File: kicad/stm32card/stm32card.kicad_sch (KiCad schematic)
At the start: 48 parts, among them SW1 TSD003A04126A02, SW2 TSD003A04126A02, SW3 TSD003A04126A02, SW4 TSD003A04126A02, SW5 TSD003A04126A02, SW6 TSD003A04126A02, SW8 TSD003A04126A02, U2 MT9216, U3 N096-1608TBBIG11-H13, U4 STM32F103C8T6

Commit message: rev1a
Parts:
- removed BAT1, BAT2, BAT3, BAT4: 2997, 2997_KEY, symbol 2025-02-07_04-30-39:2997
- removed C10, C20, C6: 10uF, Capacitor_SMD:C_0603_1608Metric, symbol Device:C
- removed C21: 100nF, Capacitor_SMD:C_0603_1608Metric, symbol Device:C
- removed R3: 0, Resistor_SMD:R_0603_1608Metric, symbol Device:R
- removed SW8: TSD003A04126A02, easyeda2kicad:SW-SMD_4P-L6.0-W6.0-P4.50-LS8.6, symbol easyeda2kicad:TSD003A04126A02
- added J1: USB_C_Receptacle_PowerOnly_6P, indigos_kicad_lib:SAMESKY_UJC-H-G-SMT-2-P6-TR, symbol Connector:USB_C_Receptacle_PowerOnly_6P
- added R1, R2: 5.1k, Resistor_SMD:R_0603_1608Metric, symbol Device:R
- added SWCLK1: SWCLK, TestPoint:TestPoint_Pad_D2.0mm, symbol Connector:TestPoint
- added SWDIO1: SWDIO, TestPoint:TestPoint_Pad_D2.0mm, symbol Connector:TestPoint
- added TP1: 675_positive, TestPoint:TestPoint_Pad_4.0x4.0mm, symbol Connector:TestPoint
- added TP_mosi1, TP_sck1: TestPoint, TestPoint:TestPoint_Pad_D2.0mm, symbol Connector:TestPoint
- added TestPoint_gnd1: TestPoint_gnd, TestPoint:TestPoint_Pad_D2.0mm, symbol Connector:TestPoint
- added U2, U3: LM66100DCK, Package_TO_SOT_SMD:SOT-363_SC-70-6, symbol Power_Management:LM66100DCK
- added U6: ~, Library:battery_holder, symbol battery_holder:quad_675
- added tst_nrst1: tst_nrst, TestPoint:TestPoint_Pad_D2.0mm, symbol Connector:TestPoint
- added unreg_vcc1: unreg_vcc, TestPoint:TestPoint_Pad_D2.0mm, symbol Connector:TestPoint
- C1: value 4.7uF -> 10uF
- C8: value 10uF -> 2.2uF
- L1: footprint Inductor_SMD:L_0603_1608Metric -> indigos_kicad_lib:IND-SMD_L5.8-W5.2
- R3: renamed from R1; footprint Resistor_SMD:R_0603_1608Metric -> Resistor_SMD:R_0805_2012Metric
- R4: renamed from R2; value 100k 1% -> 100k .01%; footprint Resistor_SMD:R_0603_1608Metric -> Resistor_SMD:R_0805_2012Metric
- renumbered C3 to C10, C19 to C11, C17 to C15, C15 to C16, C16 to C17, C5 to C2, C4 to C3, C7 to C4, C9 to C5, C11 to C6, C2 to C9, R11 to R10, R12 to R11, R7 to R12, R9 to R13, R4 to R5, R5 to R6, R8 to R7, R10 to R8, R6 to R9, U2 to U1, U3 to U5, SW4 to b_a1, SW6 to b_b1, SW2 to b_down1, SW5 to b_left1, SW3 to b_right1, SW1 to b_up1
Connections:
- net +3V0: now also C8.2; no longer C8.1
- net GND: now also C8.1, J1.A12 (GND), J1.B12 (GND), J1.S1 (SHIELD), R1.2, R2.2, TestPoint_gnd1.1, U2.2 (GND), U3.2 (GND), U3.5 (ST), U6.1 (gnd_1), U6.2 (gnd_2), U6.3 (gnd_3), U6.4 (gnd_4); no longer C8.2
- net spi1_mosi: now also TP_mosi1.1
- net spi1_sck: now also TP_sck1.1
- net in_button_a: now reaches C17.2, b_a1.4
- net in_button_a: now also U4.26 (PB13), b_a1.3
- net in_button_b: now reaches C18.2, b_b1.4
- net in_button_b: now also U4.27 (PB14), b_b1.3
- net in_button_down: now reaches C14.2, b_down1.4
- net in_button_down: now also U4.10 (PA0-WKUP), b_down1.3
- net in_button_left: now reaches C15.2, b_left1.4
- net in_button_left: now also U4.12 (PA2), b_left1.3
- net in_button_up: now reaches C13.2, b_up1.4
- net in_button_up: now also U4.13 (PA3), b_up1.3
- net in_button_right: now reaches U4.11 (PA1)
- net in_button_right: now also C16.2, b_right1.3, b_right1.4
- net power_info: now reaches U4.25 (PB12)
- net power_info: now also U2.5 (ST)
- net at U4.34 (PA13): now also SWDIO1.1
- net at U4.37 (PA14): now also SWCLK1.1
- net at U4.42 (PB6): no longer U5.7 (CS)
- net at U4.43 (PB7): no longer U5.6 (RESET)
- net at U4.45 (PB8): no longer U5.5 (RS)
- net unregulated_vcc: now reaches C1.1, U1.1 (VIN), U1.3 (EN)
- net unregulated_vcc: now also U2.6 (VOUT), U3.6 (VOUT), unreg_vcc1.1
- net button_a: no longer names the net of U4.40 (PB4)
- net button_a: no longer b_a1.3
- net button_b: no longer names the net of U4.41 (PB5)
- net button_b: no longer b_b1.3
- net button_down renamed lcd_reset
- net lcd_reset: now also U5.6 (RESET); no longer b_down1.3
- net button_left renamed lcd_cs
- net lcd_cs: now also U5.7 (CS); no longer b_left1.3
- net button_right: no longer names the net of U4.39 (PB3)
- net button_right: no longer b_right1.3
- net button_up renamed lcd_dataselect
- net lcd_dataselect: now also U5.5 (RS); no longer b_up1.3
- net reset_button: no longer names the net of C11.1, U4.7 (NRST)
- net reset_button: now also tst_nrst1.1
- new net: TP1.1, U2.1 (VIN), U3.3 (~{CE})
- new net: J1.B5 (CC2), R1.1
- new net: J1.A9 (VBUS), J1.B9 (VBUS), U2.3 (~{CE}), U3.1 (VIN)
- new net: J1.A5 (CC1), R2.1
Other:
- moved on the sheet: C1, C10, C13, C14, C15, C16, C17, C18, C2, C3, C4, C5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

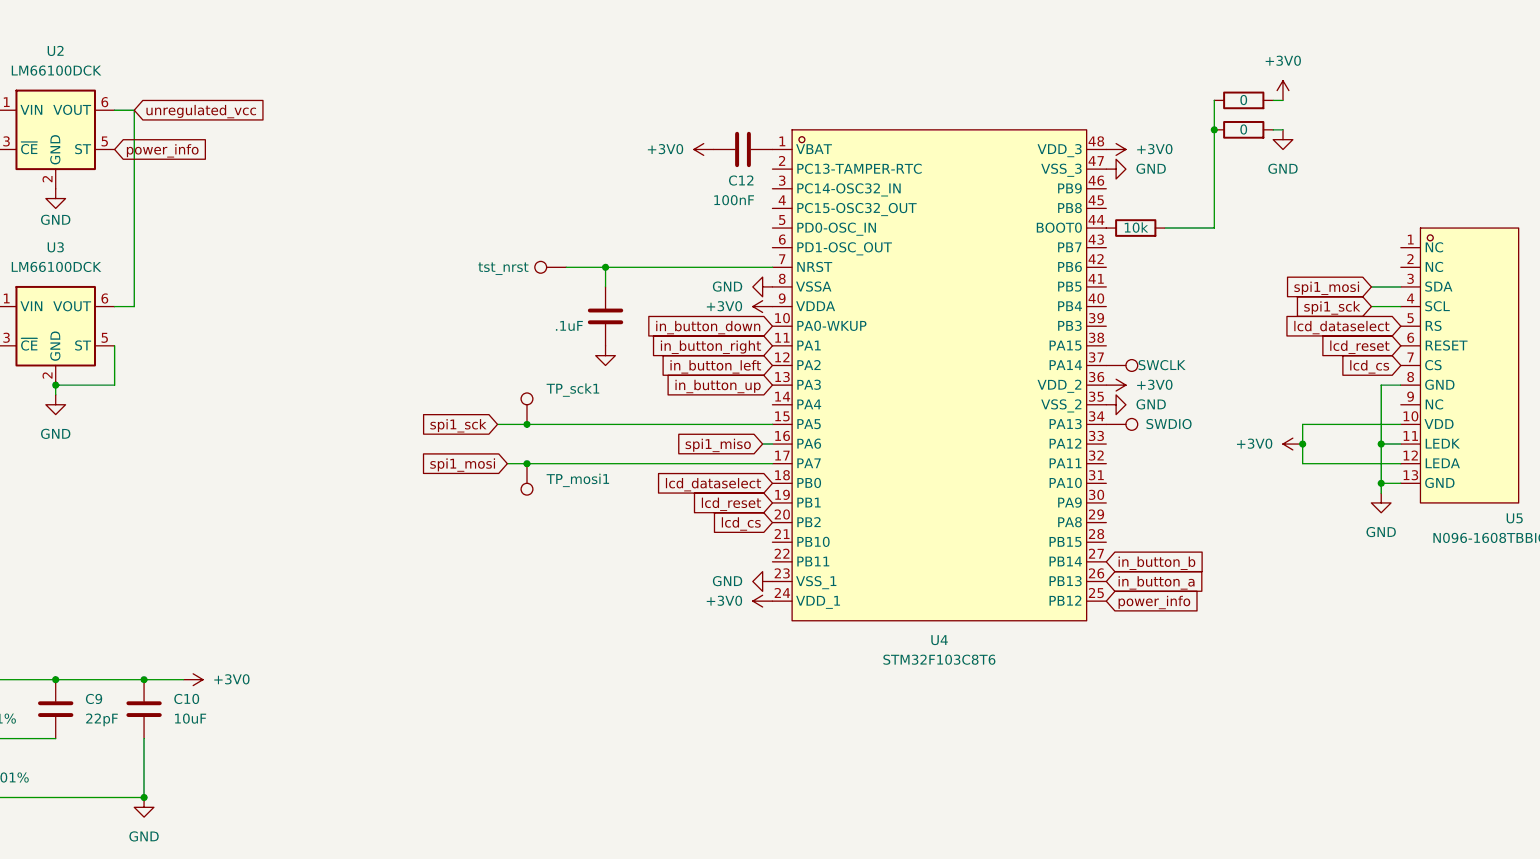
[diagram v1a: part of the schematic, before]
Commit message: optimized spi
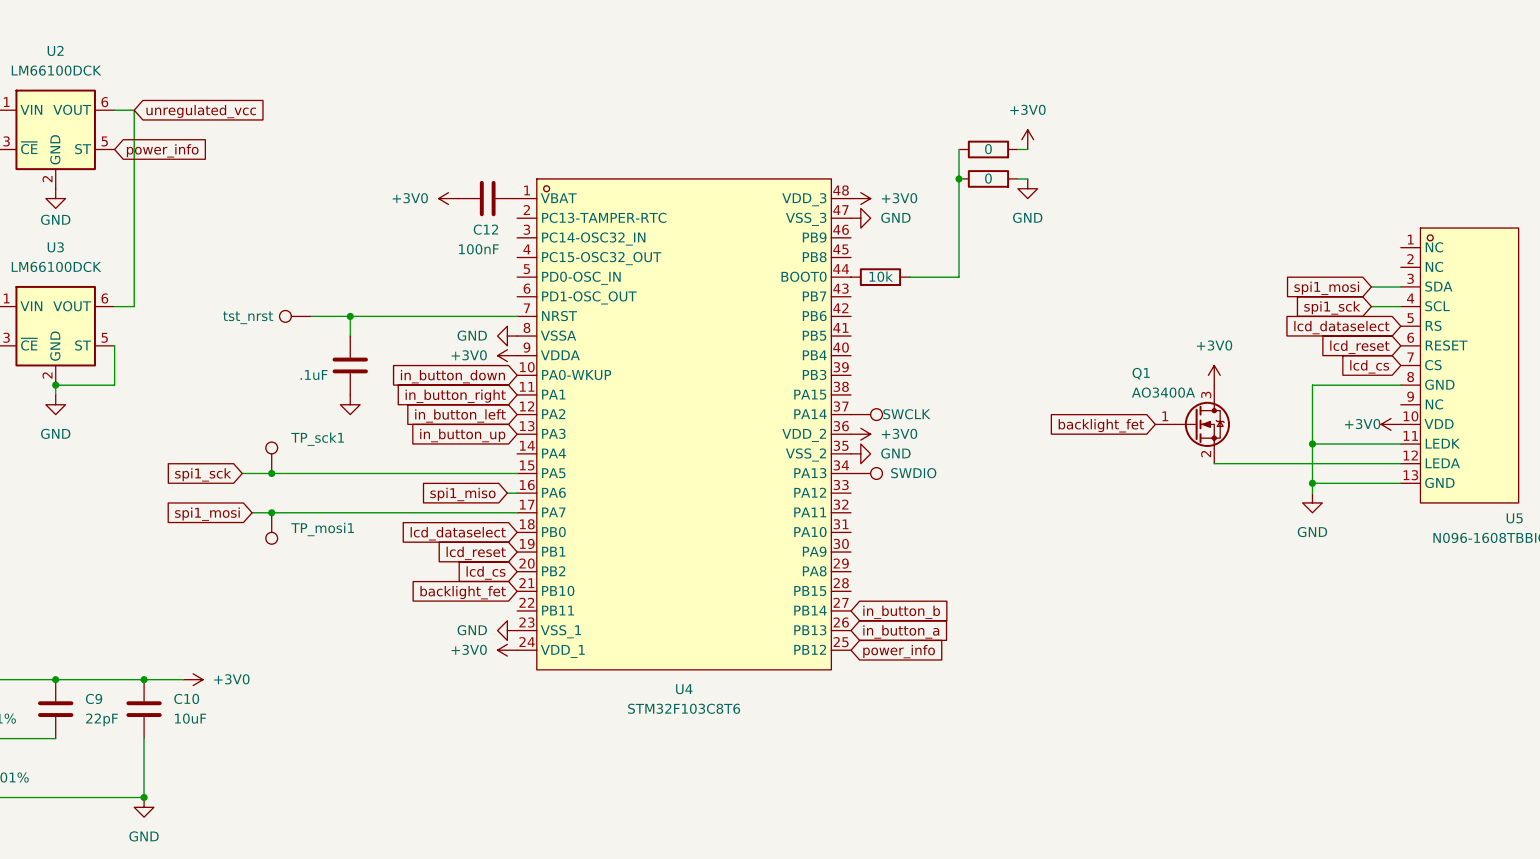
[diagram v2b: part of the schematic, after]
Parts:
- added Q1: AO3400A, Package_TO_SOT_SMD:SOT-23, symbol Transistor_FET:AO3400A
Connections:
- net +3V0: now also Q1.3 (D); no longer U5.12 (LEDA)
- net backlight_fet: now reaches U4.21 (PB10)
- net backlight_fet: now also Q1.1 (G)
- new net: Q1.2 (S), U5.12 (LEDA)
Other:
- moved on the sheet: C12, TP_mosi1, TP_sck1, U4
